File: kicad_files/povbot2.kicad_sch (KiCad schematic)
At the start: 38 parts, among them J1 GPIO, J2 Conn_01x01, J3 Conn_01x01, J4 Conn_01x02, J5 Conn_01x02, J6 Conn_01x02, Q1 BSS138, Q2 BSS138, Q3 BSS138, U1 TPS61232DRC, U4 MCP73831-2ACI_MC, U5 TB6612FNG

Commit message: floorplanning done
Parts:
- J4: footprint Connector_JST:JST_PH_S2B-PH-K_1x02_P2.00mm_Horizontal -> Connector_Molex:Molex_PicoBlade_53398-0271_1x02-1MP_P1.25mm_Vertical
- J5, J6: footprint Connector_JST:JST_PH_S2B-PH-K_1x02_P2.00mm_Horizontal -> Connector_Molex:Molex_PicoBlade_53261-0271_1x02-1MP_P1.25mm_Horizontal
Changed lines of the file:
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@@
       (effects (font (size 1.27 1.27)))
     )
-    (property "Footprint" "Connector_JST:JST_PH_S2B-PH-K_1x02_P2.00mm_Horizontal" (at 107.95 179.07 0)
+    (property "Footprint" "Connector_Molex:Molex_PicoBlade_53261-0271_1x02-1MP_P1.25mm_Horizontal" (at 107.95 179.07 0)
       (effects (font (size 1.27 1.27)) hide)
     )
@@
       (effects (font (size 1.27 1.27)) (justify left))
     )
-    (property "Footprint" "Connector_JST:JST_PH_S2B-PH-K_1x02_P2.00mm_Horizontal" (at 92.71 176.53 0)
+    (property "Footprint" "Connector_Molex:Molex_PicoBlade_53398-0271_1x02-1MP_P1.25mm_Vertical" (at 92.71 176.53 0)
       (effects (font (size 1.27 1.27)) hide)
     )
@@
       (effects (font (size 1.27 1.27)))
     )
-    (property "Footprint" "Connector_JST:JST_PH_S2B-PH-K_1x02_P2.00mm_Horizontal" (at 138.43 179.07 0)
-      (effects (font (size 1.27 1.27)) hide)
-    )
+    (property "Footprint" "Connector_Molex:Molex_PicoBlade_53261-0271_1x02-1MP_P1.25mm_Horizontal" (at 138.43 179.07 0)
+      (effects (font (size 1.27 1.27)) hide)
+    )

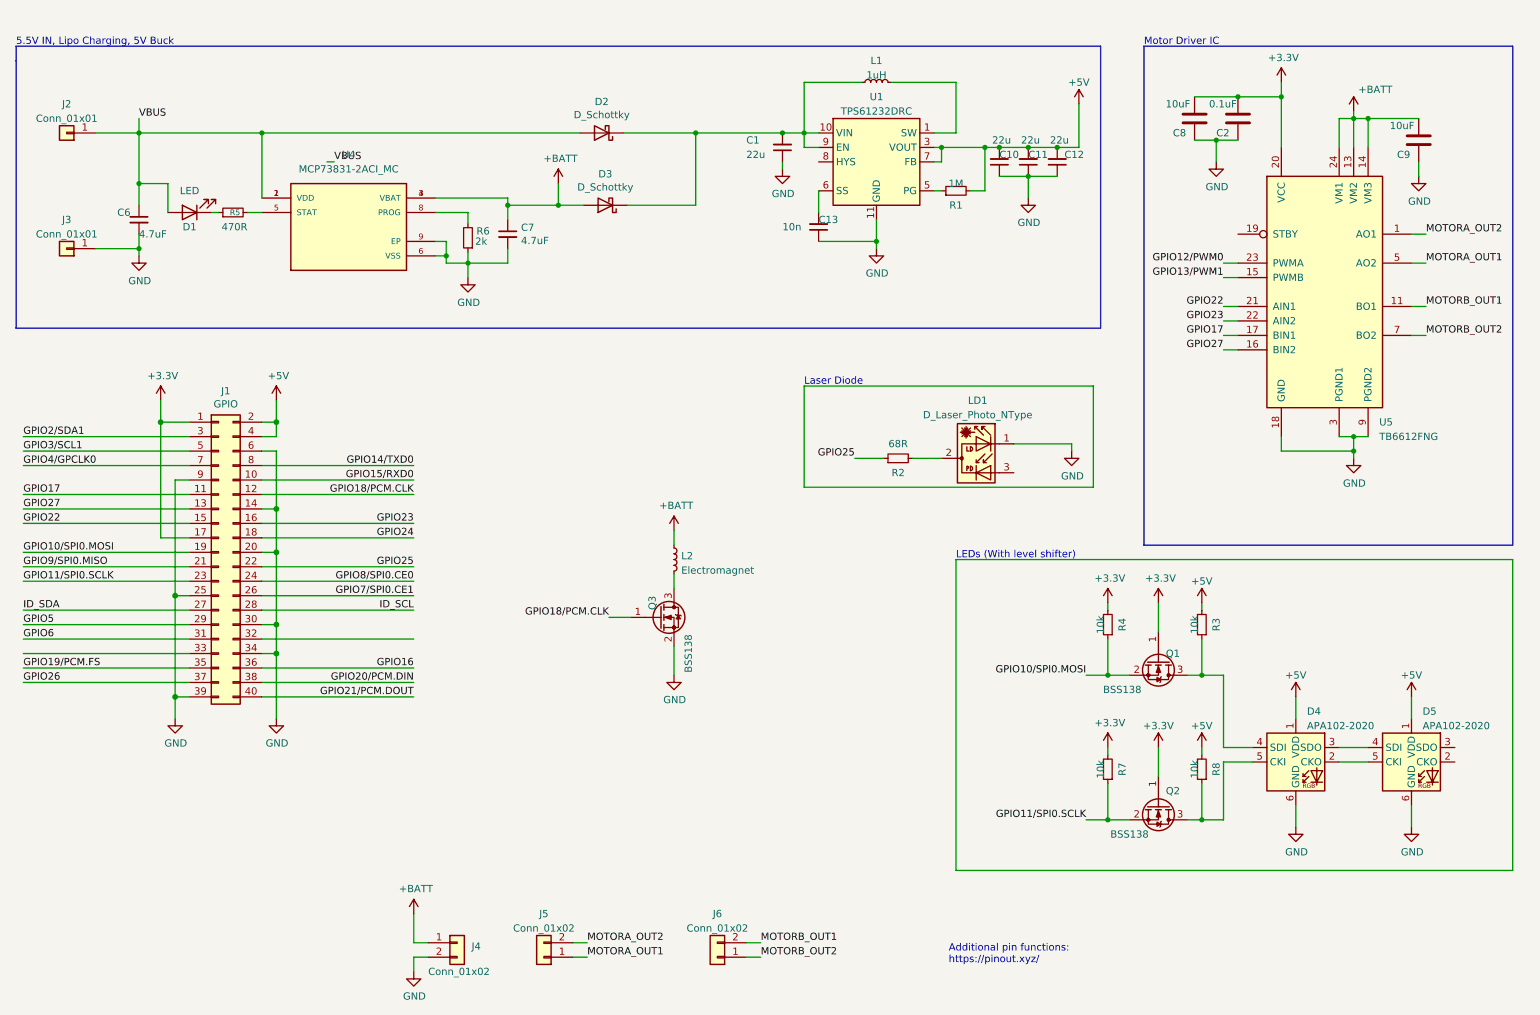
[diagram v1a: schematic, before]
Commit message: changed inductor larger package 5A current version, made pcbway fab files
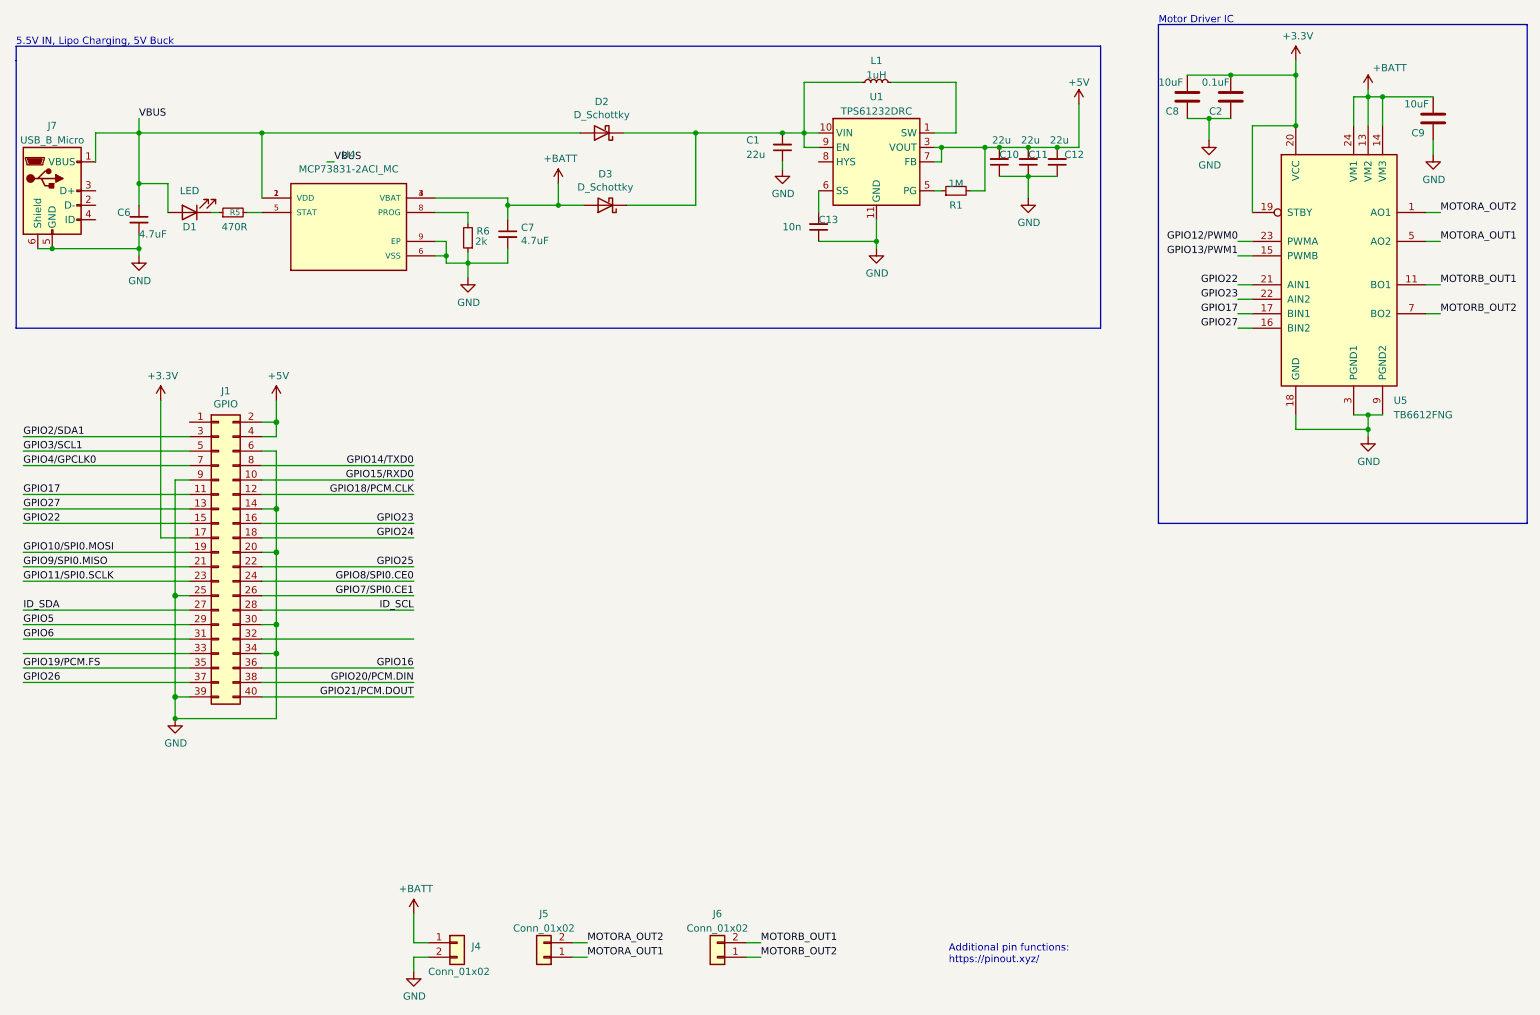
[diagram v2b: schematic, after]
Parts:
- removed D4, D5: APA102-2020, LED_SMD:LED-APA102-2020, symbol LED:APA102-2020
- removed J2, J3: Conn_01x01, Connector_PinHeader_2.54mm:PinHeader_1x01_P2.54mm_Vertical, symbol Connector_Generic:Conn_01x01
- removed L2: Electromagnet, Connector_PinHeader_2.54mm:PinHeader_1x02_P2.54mm_Vertical, symbol Device:L_Small
- removed LD1: D_Laser_Photo_NType, OptoDevice:LaserDiode_TO18-D5.6-3, symbol Device:D_Laser_Photo_NType
- removed Q1, Q2, Q3: BSS138, Package_TO_SOT_SMD:SOT-23, symbol Transistor_FET:BSS138
- removed R2: 68R, Resistor_SMD:R_0603_1608Metric, symbol Device:R_Small
- removed R3, R4, R7, R8: 10k, Resistor_SMD:R_0603_1608Metric, symbol Device:R_Small
- added J7: USB_B_Micro, Connector_USB:USB_Micro-B_Molex_47346-0001, symbol Connector:USB_B_Micro
- C1: footprint (none) -> Capacitor_SMD:C_0603_1608Metric
- C13: footprint Capacitor_SMD:C_0402_1005Metric -> Capacitor_SMD:C_0603_1608Metric
- D1: footprint LED_SMD:LED_0402_1005Metric -> LED_SMD:LED_0603_1608Metric
- D2, D3: MPN (none) -> SBA120CS_R1_00001
- J1: MPN (none) -> 61304021121
- J4: footprint Connector_Molex:Molex_PicoBlade_53398-0271_1x02-1MP_P1.25mm_Vertical -> Connector_JST:JST_PH_B2B-PH-K_1x02_P2.00mm_Vertical; MPN (none) -> B2B-PH-K-S
- J5, J6: footprint Connector_Molex:Molex_PicoBlade_53261-0271_1x02-1MP_P1.25mm_Horizontal -> Connector_JST:JST_PH_B2B-PH-K_1x02_P2.00mm_Vertical; MPN (none) -> B2B-PH-K-S
- L1: footprint Inductor_SMD:L_0402_1005Metric -> Kicad_parts:IND_SRP4020TA-1R0M; MPN (none) -> SRP4020TA-1R0M
- U1: MPN (none) -> TPS61232DRCR
- U4: footprint kicad_footprints:SON50P200X300X100-9N -> Kicad_parts:SON50P200X300X100-9N; MPN (none) -> MCP73831-2ACI/MC
- U5: LCSC (none) -> C141517; MPN (none) -> TB6612FNG,C,8,EL
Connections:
- net +3V3: now also U5.19 (STBY); no longer J1.1 (Pin_1)
- net GND: now also J7.5 (GND), J7.6 (Shield)
- net VBUS: now also J7.1 (VBUS)
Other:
- note removed: "LEDs (With level shifter)"
- note removed: "Laser Diode"
- moved on the sheet: C2, C8, C9, U5
